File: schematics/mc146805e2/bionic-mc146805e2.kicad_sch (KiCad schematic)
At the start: 8 parts, among them J1 Bionic-P135, J2 Bionic-P245, U1 MC146805E2P, U2 11AA010-I/TT

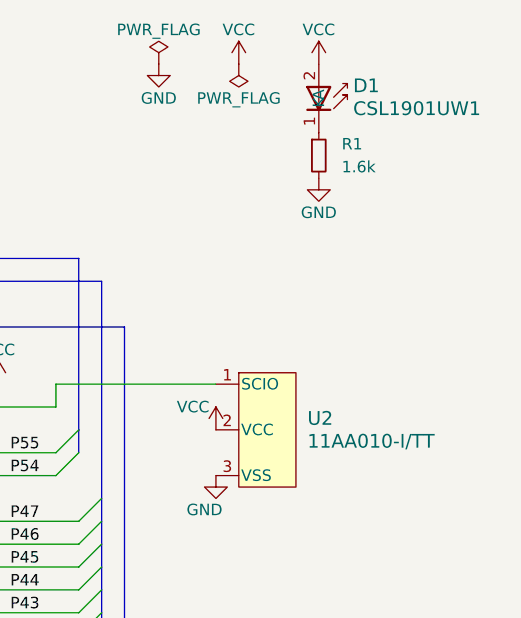
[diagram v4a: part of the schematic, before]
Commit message: [MC146805E2] Cleanup schematics
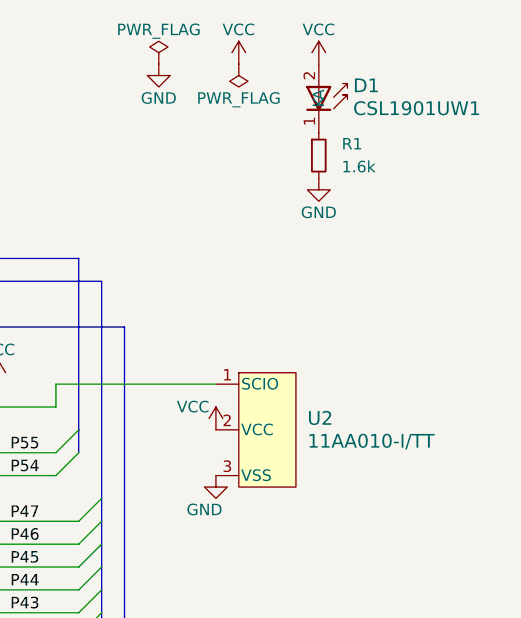
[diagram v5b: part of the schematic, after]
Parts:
- D1: footprint 0-LocalLibrary:LED_CSL1901UW1_ROM-M -> rhom:LED_CSL1901UW1_ROM-M; symbol 0-LocalLibrary:CSL1901UW1 -> rhom:CSL1901UW1
- J1: footprint 0-LocalLibrary:Bionic-P135_Vertical -> bionic:Bionic-P135_Vertical; symbol 0-LocalLibrary:Bionic-P135 -> bionic:Bionic-P135
- J2: footprint 0-LocalLibrary:Bionic-P245_Vertical -> bionic:Bionic-P245_Vertical; symbol 0-LocalLibrary:Bionic-P245 -> bionic:Bionic-P245
- U1: footprint 0-LocalLibrary:DIP-40_W15.24mm_Socket -> bionic:DIP-40_W15.24mm_Socket; symbol 0-LocalLibrary:MC146805E2P -> cpu:MC146805E2P
- U2: footprint 0-LocalLibrary:SOT-23_MC_MCH-M -> microchip:SOT-23_MC_MCH-M; symbol 0-LocalLibrary:11AA010-I_TT -> microchip:11AA010-I_TT
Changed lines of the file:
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@@
 	)
 	(symbol
-		(lib_id "0-LocalLibrary:MC146805E2P")
+		(lib_id "cpu:MC146805E2P")
 		(at 92.71 107.95 0)
 		(unit 1)
@@
 			)
 		)
-		(property "Footprint" "0-LocalLibrary:DIP-40_W15.24mm_Socket"
+		(property "Footprint" "bionic:DIP-40_W15.24mm_Socket"
 			(at 93.98 142.24 0)
 			(effects
@@
 			)
 		)
-		(property "Description" ""
+		(property "Description" "8-bit General Purpose Microprocessor, DIP-40"
 			(at 92.71 107.95 0)
 			(effects
@@
 	)
 	(symbol
-		(lib_id "0-LocalLibrary:CSL1901UW1")
+		(lib_id "rhom:CSL1901UW1")
 		(at 203.2 41.91 270)
 		(unit 1)
@@
 		(fields_autoplaced yes)
 		(property "Reference" "D1"
-			(at 207.01 44.323 90)
+			(at 207.01 44.3229 90)
 			(effects
 				(font
@@
 		)
 		(property "Value" "CSL1901UW1"
-			(at 207.01 46.863 90)
+			(at 207.01 46.8629 90)
 			(effects
 				(font
@@
 			)
 		)
-		(property "Footprint" "0-LocalLibrary:LED_CSL1901UW1_ROM-M"
+		(property "Footprint" "rhom:LED_CSL1901UW1_ROM-M"
 			(at 194.31 45.72 0)
 			(effects
@@
 	)
 	(symbol
-		(lib_id "0-LocalLibrary:Bionic-P135")
+		(lib_id "bionic:Bionic-P135")
 		(at 157.48 105.41 0)
 		(unit 1)
@@
 			)
 		)
-		(property "Footprint" "0-LocalLibrary:Bionic-P135_Vertical"
+		(property "Footprint" "bionic:Bionic-P135_Vertical"
 			(at 158.75 140.97 0)
 			(effects
@@
 			)
 		)
-		(property "Description" ""
+		(property "Description" "Generic connector, single row, 01x24, script generated (kicad-library-utils/schlib/autogen/connector/)"
 			(at 157.48 105.41 0)
 			(effects
@@
 	)
 	(symbol
-		(lib_id "0-LocalLibrary:Bionic-P245")
+		(lib_id "bionic:Bionic-P245")
 		(at 165.1 105.41 0)
 		(unit 1)
@@
 			)
 		)
-		(property "Footprint" "0-LocalLibrary:Bionic-P245_Vertical"
+		(property "Footprint" "bionic:Bionic-P245_Vertical"
 			(at 166.37 140.97 0)
 			(effects
@@
 			)
 		)
-		(property "Description" ""
+		(property "Description" "Generic connector, single row, 01x24, script generated (kicad-library-utils/schlib/autogen/connector/)"
 			(at 165.1 105.41 0)
 			(effects
@@
 	)
 	(symbol
-		(lib_id "0-LocalLibrary:11AA010-I_TT")
+		(lib_id "microchip:11AA010-I_TT")
 		(at 194.31 76.2 0)
 		(unit 1)
@@
 		(fields_autoplaced yes)
 		(property "Reference" "U2"
-			(at 201.93 81.28 0)
+			(at 201.93 81.2799 0)
 			(effects
 				(font
@@
 		)
 		(property "Value" "11AA010-I/TT"
-			(at 201.93 83.82 0)
+			(at 201.93 83.8199 0)
 			(effects
 				(font
@@
 			)
 		)
-		(property "Footprint" "0-LocalLibrary:SOT-23_MC_MCH-M"
+		(property "Footprint" "microchip:SOT-23_MC_MCH-M"
 			(at 196.85 93.98 0)
 			(effects
@@
 			)
 		)
-		(property "Description" ""
+		(property "Description" "UNI/O Serial EEPROM (1Kbit)"
 			(at 194.31 76.2 0)
 			(effects

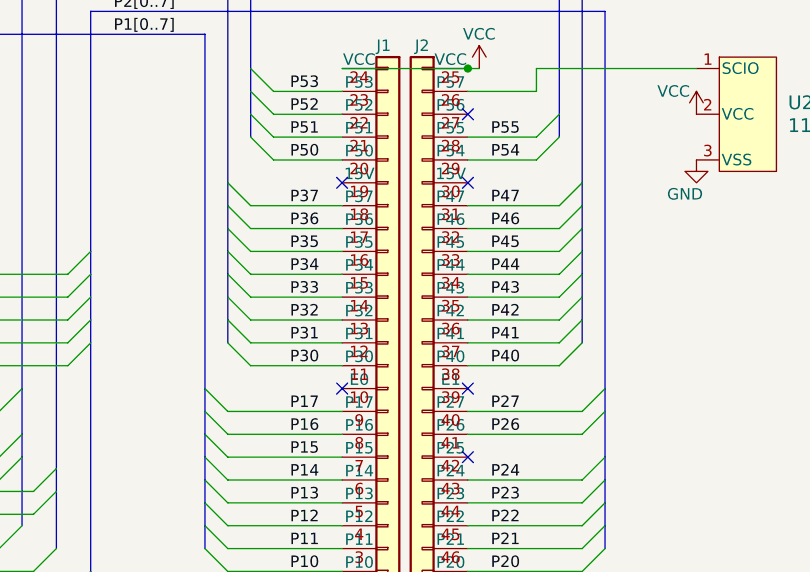
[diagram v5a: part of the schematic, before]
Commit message: [MC146805E2] Update schematics
Remove unused pins from bionic connector
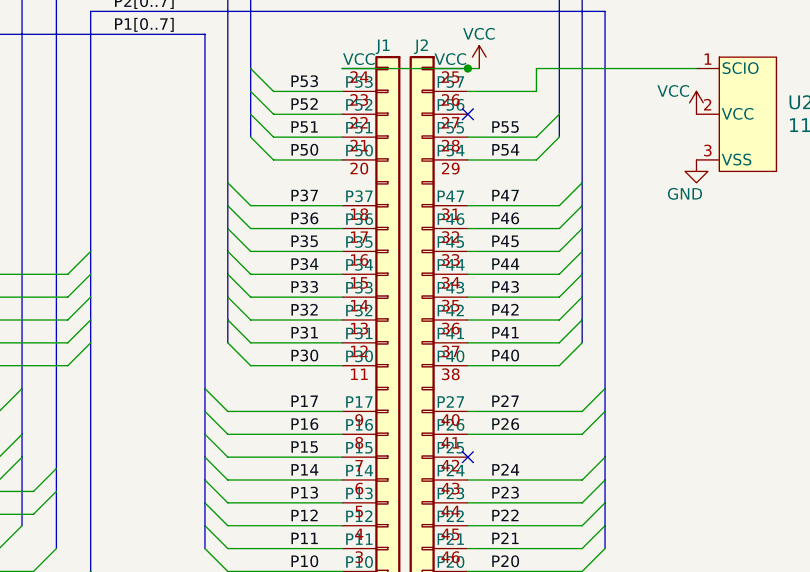
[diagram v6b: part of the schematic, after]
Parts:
- J1: footprint bionic:Bionic-P135_Vertical -> bionic:Bionic-P135_THT
- J2: footprint bionic:Bionic-P245_Vertical -> bionic:Bionic-P245_THT
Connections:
- no-connect marks 7 -> 3
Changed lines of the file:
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@@
 	(title_block
 		(title "BionicMC146805E2")
-		(date "2024-12-01")
-		(rev "8")
+		(date "2025-03-02")
+		(rev "9")
 		(company "Tadashi G. Takaoka")
 	)
@@
 	)
 	(no_connect
-		(at 152.4 90.17)
-	)
-	(no_connect
-		(at 166.37 113.03)
-	)
-	(no_connect
-		(at 166.37 90.17)
-	)
-	(no_connect
-		(at 152.4 113.03)
-	)
-	(no_connect
 		(at 166.37 120.65)
 	)
@@
 			)
 		)
-		(property "Footprint" "bionic:Bionic-P135_Vertical"
+		(property "Footprint" "bionic:Bionic-P135_THT"
 			(at 158.75 140.97 0)
 			(effects
@@
 		(pin "21"
 		)
-		(pin "19"
-		)
 		(pin "4"
 		)
-		(pin "10"
-		)
 		(pin "2"
 		)
@@
 			)
 		)
-		(property "Footprint" "bionic:Bionic-P245_Vertical"
+		(property "Footprint" "bionic:Bionic-P245_THT"
 			(at 166.37 140.97 0)
 			(effects
@@
 		(pin "40"
 		)
-		(pin "30"
-		)
 		(pin "48"
 		)
@@
 		(pin "42"
 		)
-		(pin "39"
-		)
 		(pin "25"
